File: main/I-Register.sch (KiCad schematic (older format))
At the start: 19 parts, among them U4 74LS245, U5 74LS173, U6 74LS173

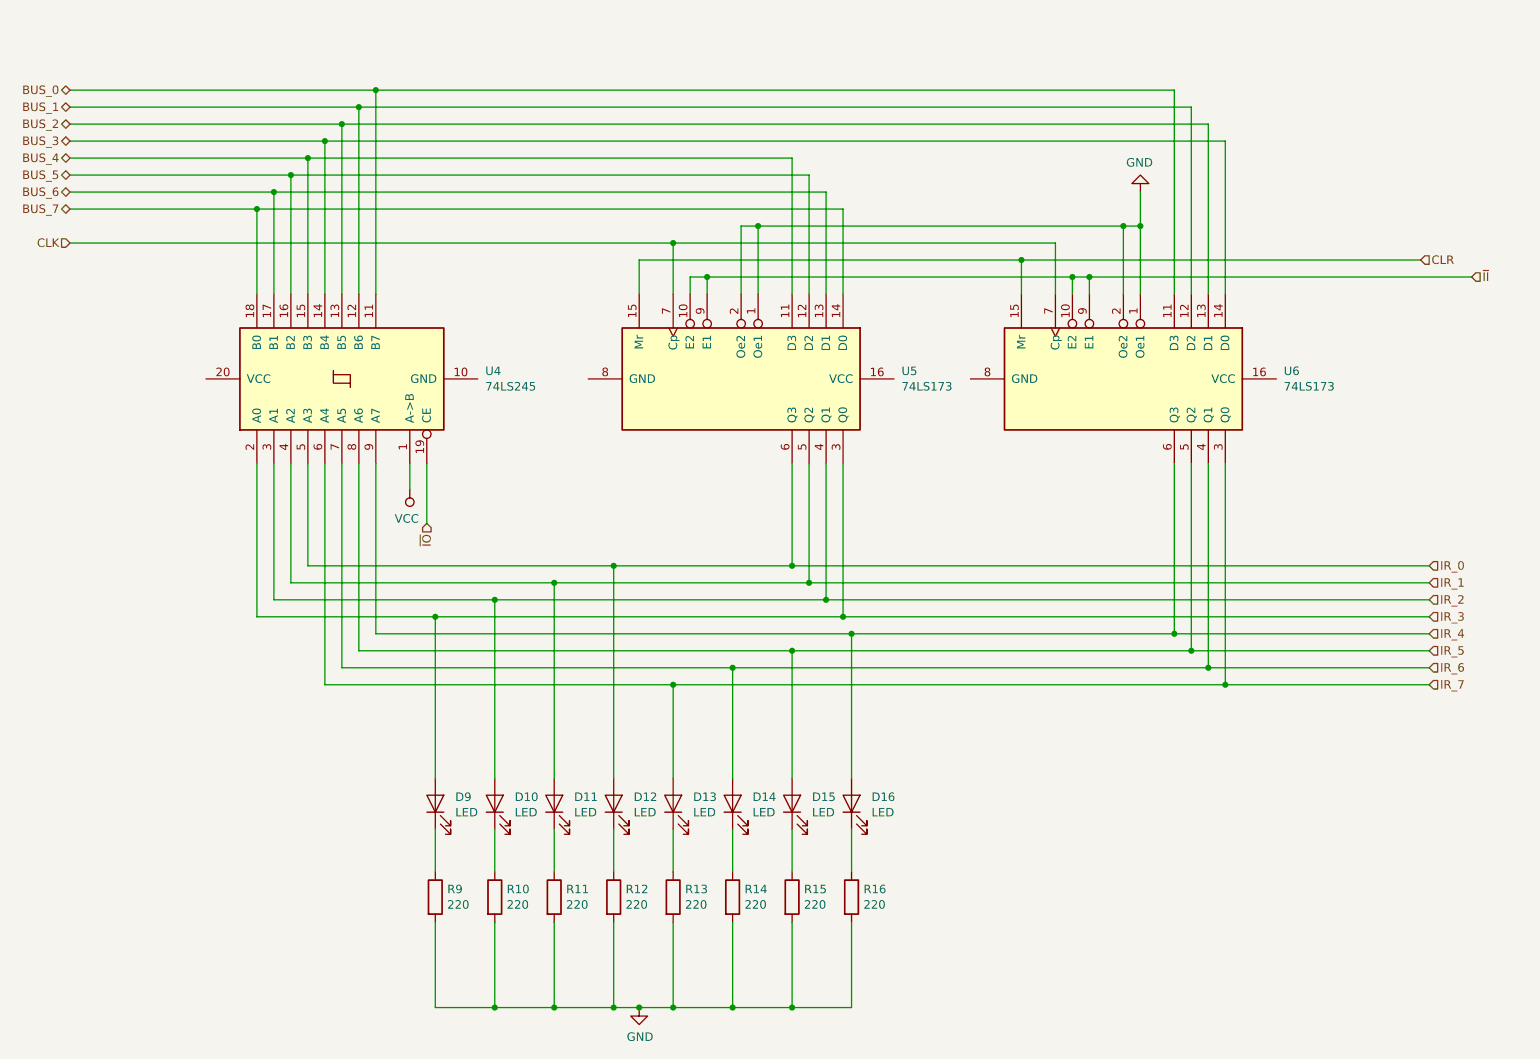
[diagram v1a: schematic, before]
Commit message: Switch to using 74LS377 in place of two 74LS173
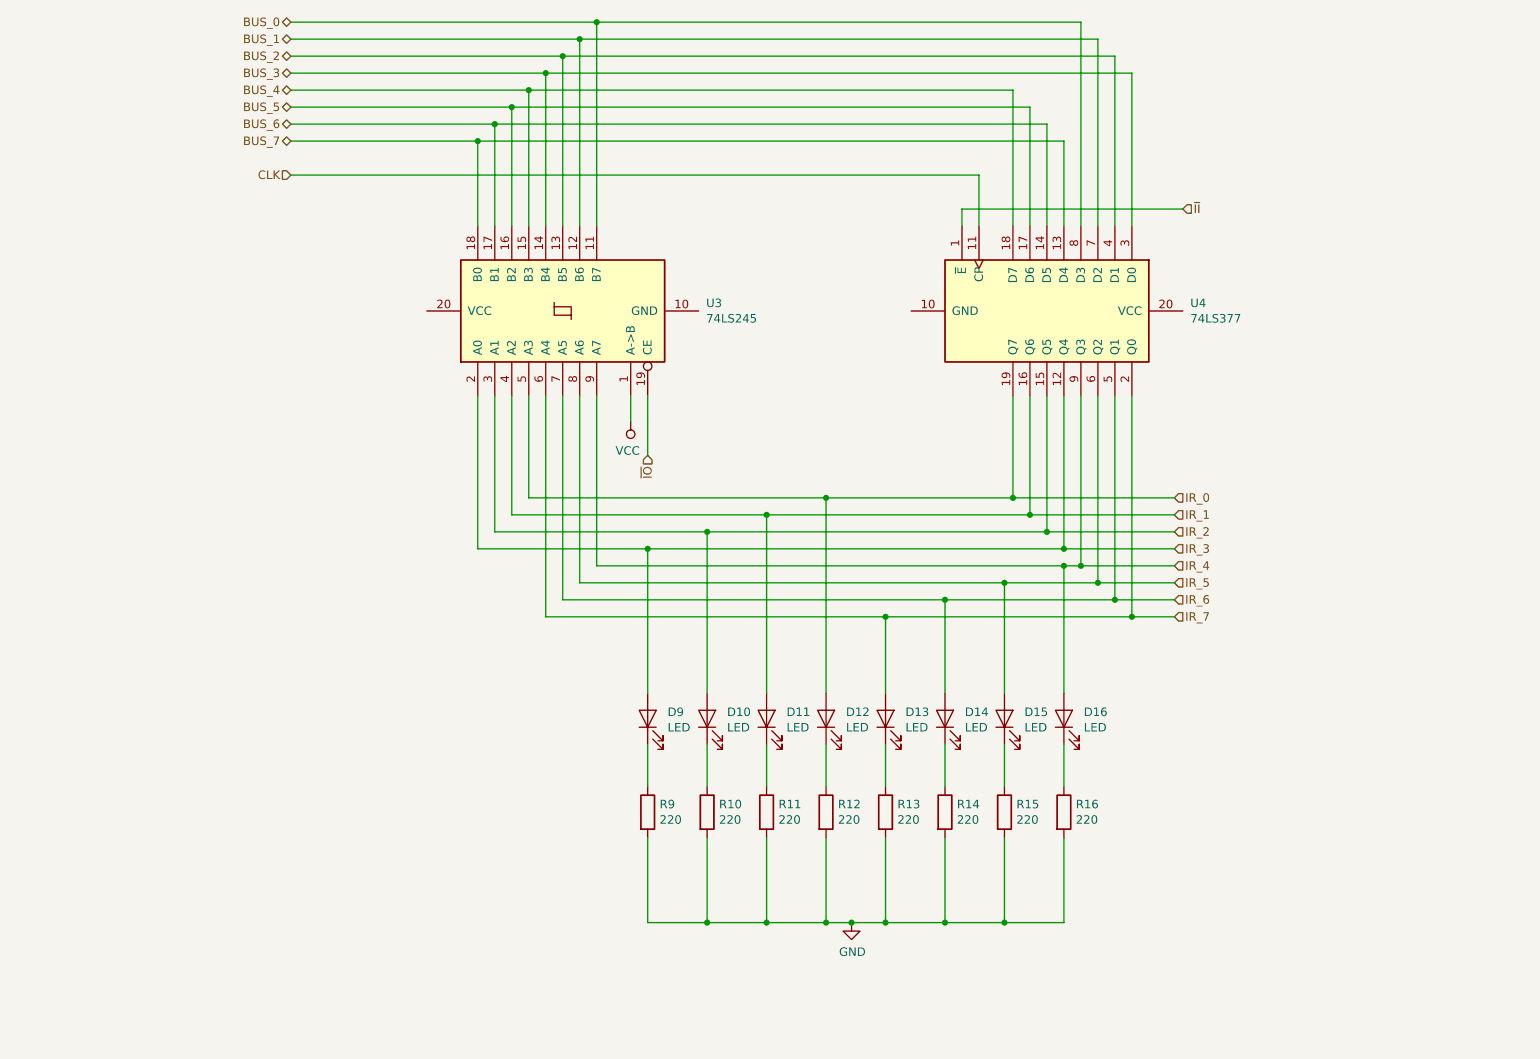
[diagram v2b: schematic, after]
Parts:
- removed U4: 74LS245, symbol 74xx:74LS245
- removed U5, U6: 74LS173, symbol 74xx:74LS173
- added U3: 74LS245, symbol 74xx:74LS245
- added U4: 74LS377, symbol 74xx:74LS377
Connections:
- net BUS_0: now also U3.11 (B7), U4.8 (D3)
- net BUS_1: now also U3.12 (B6), U4.7 (D2)
- net BUS_2: now also U3.13 (B5), U4.4 (D1)
- net BUS_3: now also U3.14 (B4), U4.3 (D0)
- net BUS_4: now also U3.15 (B3), U4.18 (D7)
- net BUS_5: now also U3.16 (B2), U4.17 (D6)
- net BUS_6: now also U3.17 (B1), U4.14 (D5)
- net BUS_7: now also U3.18 (B0), U4.13 (D4)
- net CLK: now also U4.11 (CP)
- net IR_0: now also U3.5 (A3), U4.19 (Q7)
- net IR_1: now also U3.4 (A2), U4.16 (Q6)
- net IR_2: now also U3.3 (A1), U4.15 (Q5)
- net IR_3: now also U3.2 (A0), U4.12 (Q4)
- net IR_4: now also U3.9 (A7), U4.9 (Q3)
- net IR_5: now also U3.8 (A6), U4.6 (Q2)
- net IR_6: now also U3.7 (A5), U4.5 (Q1)
- net IR_7: now also U3.6 (A4), U4.2 (Q0)
- net VCC: now also U3.1 (A->B)
- net ~II~: now also U4.1 (~E)
- net ~IO~: now also U3.19 (CE)
